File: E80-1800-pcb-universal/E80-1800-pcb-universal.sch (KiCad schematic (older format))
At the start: 48 parts, among them J1 SPI, J2 BATT, J3 OLED, J4 USB_C_Receptacle_USB2.0, Q1 AO3400A, SW1 RST, SW2 BOOT, U1 SRV05-4, U2 XC6206P332MR, U3 STM32F072RBTx

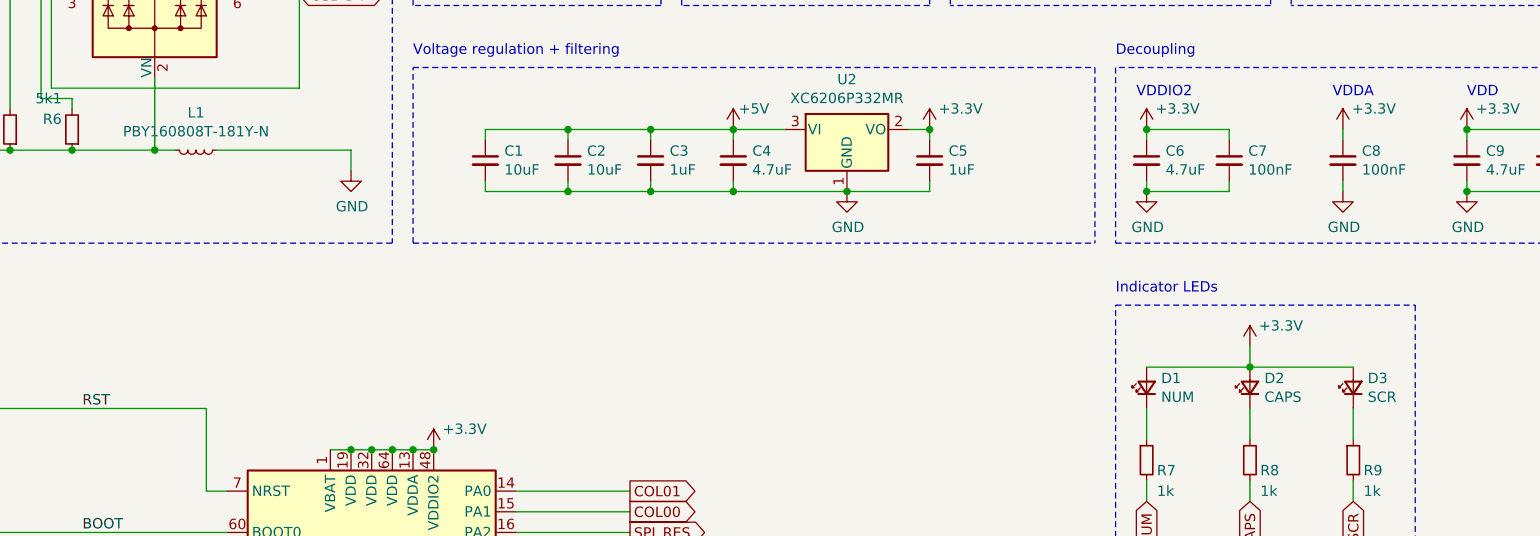
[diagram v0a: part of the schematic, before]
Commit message: added TVS for ESD prot
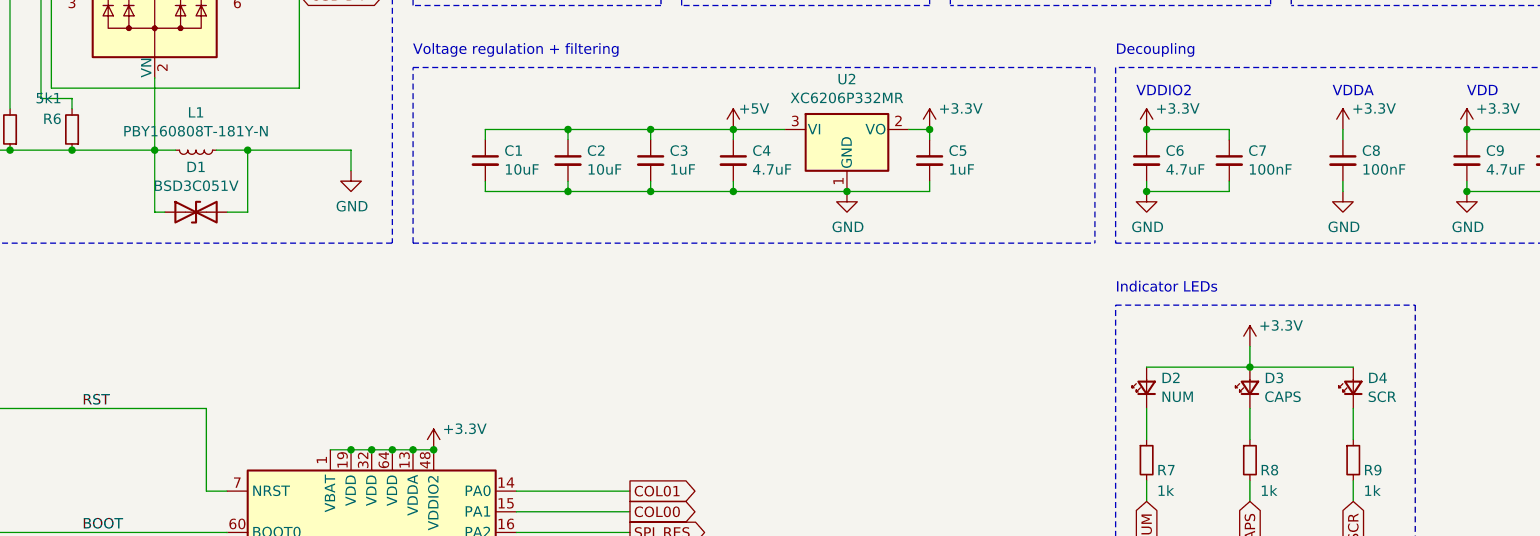
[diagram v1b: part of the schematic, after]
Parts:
- added D1: BSD3C051V, Diode_SMD:D_SOD-323, symbol Device:D_TVS
- renumbered D1 to D2, D2 to D3, D3 to D4
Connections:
- net Earth: now also D1.1 (A1)
- net GND: now also D1.2 (A2)
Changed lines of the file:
@@
 	3400 2600 3400 2500
 Wire Wire Line
-	2750 2500 3400 2500
+	2750 2500 2900 2500
 Wire Wire Line
 	1650 1750 1950 1750
@@
 $EndComp
 $Comp
-L Device:LED_Small D1
+L Device:LED_Small D2
 U 1 1 5F118BDD
 P 7250 3650
-F 0 "D1" V 7296 3580 50  0000 R CNN
+F 0 "D2" V 7296 3580 50  0000 R CNN
 F 1 "NUM" V 7205 3580 50  0000 R CNN
 F 2 "LED_THT:LED_D3.0mm" H 7250 3650 50  0001 C CNN
@@
 $EndComp
 $Comp
-L Device:LED_Small D2
+L Device:LED_Small D3
 U 1 1 5F11A25F
 P 7750 3650
-F 0 "D2" V 7796 3580 50  0000 R CNN
+F 0 "D3" V 7796 3580 50  0000 R CNN
 F 1 "CAPS" V 7705 3580 50  0000 R CNN
 F 2 "LED_THT:LED_D3.0mm" H 7750 3650 50  0001 C CNN
@@
 $EndComp
 $Comp
-L Device:LED_Small D3
+L Device:LED_Small D4
 U 1 1 5F11A8DA
 P 8250 3650
-F 0 "D3" V 8296 3580 50  0000 R CNN
+F 0 "D4" V 8296 3580 50  0000 R CNN
 F 1 "SCR" V 8205 3580 50  0000 R CNN
 F 2 "LED_THT:LED_D3.0mm" H 8250 3650 50  0001 C CNN
@@
 F1 "E80-1800-Matrix.sch" 50
 $EndSheet
+$Comp
+L Device:D_TVS D1
+U 1 1 5F7B071F
+P 2650 2800
+F 0 "D1" H 2650 3017 50  0000 C CNN
+F 1 "BSD3C051V" H 2650 2926 50  0000 C CNN
+F 2 "Diode_SMD:D_SOD-323" H 2650 2800 50  0001 C CNN
+F 3 "https://datasheet.lcsc.com/szlcsc/Bourne-Semicon-Shenzhen-BSD3C051V_C151996.pdf" H 2650 2800 50  0001 C CNN
+F 4 "C151996" H 2650 2800 50  0001 C CNN "LCSC"
+	1    2650 2800
+	1    0    0    -1
+$EndComp
+Wire Wire Line
+	2450 2500 2450 2800
+Wire Wire Line
+	2450 2800 2500 2800
+Wire Wire Line
+	2800 2800 2900 2800
+Wire Wire Line
+	2900 2800 2900 2500
+Connection ~ 2900 2500
+Wire Wire Line
+	2900 2500 3400 2500
 $EndSCHEMATC

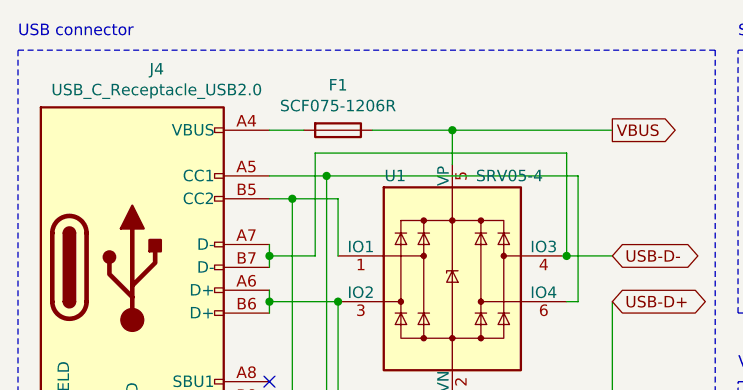
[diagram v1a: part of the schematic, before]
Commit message: swapped parts to fit jlc stocks
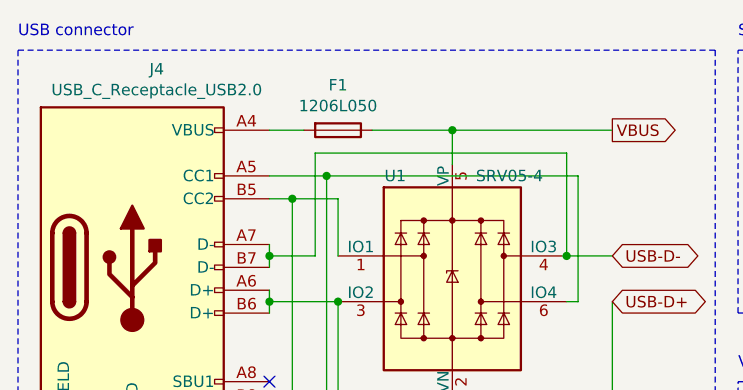
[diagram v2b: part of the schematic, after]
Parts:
- F1: value SCF075-1206R -> 1206L050; footprint Fuse:Fuse_1206_3216Metric_Pad1.42x1.75mm_HandSolder -> Fuse:Fuse_1206_3216Metric; LCSC C183290 -> C151162
- Q1: LCSC C20917 -> C347475
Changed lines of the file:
@@
 F 2 "kicad-keyboard-parts:SOT-23_stealth" H 9050 1350 50  0001 C CNN
 F 3 "https://datasheet.lcsc.com/szlcsc/Alpha-Omega-Semicon-AOS-AO3400A_C20917.pdf" H 8850 1250 50  0001 C CNN
-F 4 "C20917" H 8850 1250 50  0001 C CNN "LCSC"
+F 4 "C347475" H 8850 1250 50  0001 C CNN "LCSC"
 	1    8850 1250
 	1    0    0    -1
@@
 P 1950 1000
 F 0 "F1" V 1753 1000 50  0000 C CNN
-F 1 "SCF075-1206R" V 1844 1000 50  0000 C CNN
-F 2 "Fuse:Fuse_1206_3216Metric_Pad1.42x1.75mm_HandSolder" V 1880 1000 50  0001 C CNN
-F 3 "~" H 1950 1000 50  0001 C CNN
-F 4 "C183290" H 1950 1000 50  0001 C CNN "LCSC"
+F 1 "1206L050" V 1844 1000 50  0000 C CNN
+F 2 "Fuse:Fuse_1206_3216Metric" V 1880 1000 50  0001 C CNN
+F 3 "https://datasheet.lcsc.com/szlcsc/1810171711_Littelfuse-1206L050-15YR_C151162.pdf" H 1950 1000 50  0001 C CNN
+F 4 "C151162" H 1950 1000 50  0001 C CNN "LCSC"
 	1    1950 1000
 	0    1    1    0

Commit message: updated kicad cpl/bom to match current stocks, cleaned some unneeded files
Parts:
- J4: LCSC (none) -> C165948
- Q1: LCSC C347475 -> C20917
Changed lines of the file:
@@
 F 2 "kicad-keyboard-parts:SOT-23_stealth" H 9050 1350 50  0001 C CNN
 F 3 "https://datasheet.lcsc.com/szlcsc/Alpha-Omega-Semicon-AOS-AO3400A_C20917.pdf" H 8850 1250 50  0001 C CNN
-F 4 "C347475" H 8850 1250 50  0001 C CNN "LCSC"
+F 4 "C20917" H 8850 1250 50  0001 C CNN "LCSC"
 	1    8850 1250
 	1    0    0    -1
@@
 F 2 "Connector_USB:USB_C_Receptacle_HRO_TYPE-C-31-M-12" H 1200 1600 50  0001 C CNN
 F 3 "https://www.usb.org/sites/default/files/documents/usb_type-c.zip" H 1200 1600 50  0001 C CNN
+F 4 " C165948" H 1050 1600 50  0001 C CNN "LCSC"
 	1    1050 1600
 	1    0    0    -1
